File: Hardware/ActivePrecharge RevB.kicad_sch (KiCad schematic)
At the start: 59 parts, among them J1 HVConnector, J2 PrechargeContactor, J3 MainContactor, J4 ExportConnector, J5 HV+, J6 HV-, J7 Conn_01x02_Pin, U1 TLV9002QDRQ1, U2 LT1963AEST-3.3#TRPBF

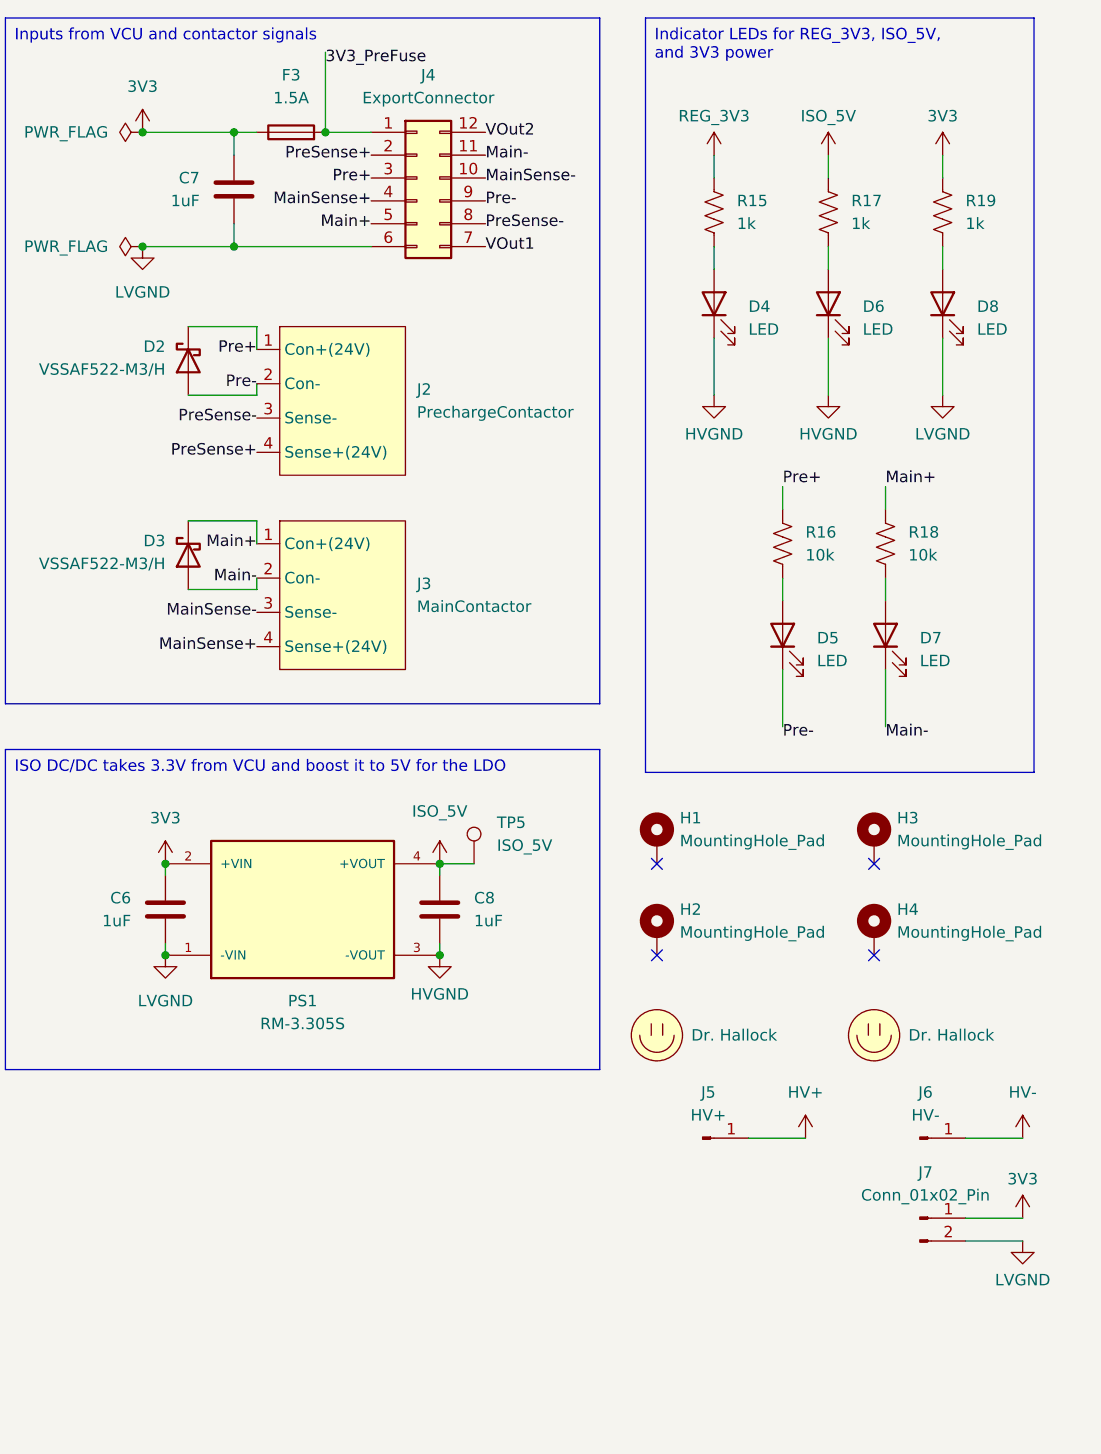
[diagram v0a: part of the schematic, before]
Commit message: HV Fuse update (#18)
* changed fuses to be HV fuses

* add step file

* silk screen updates
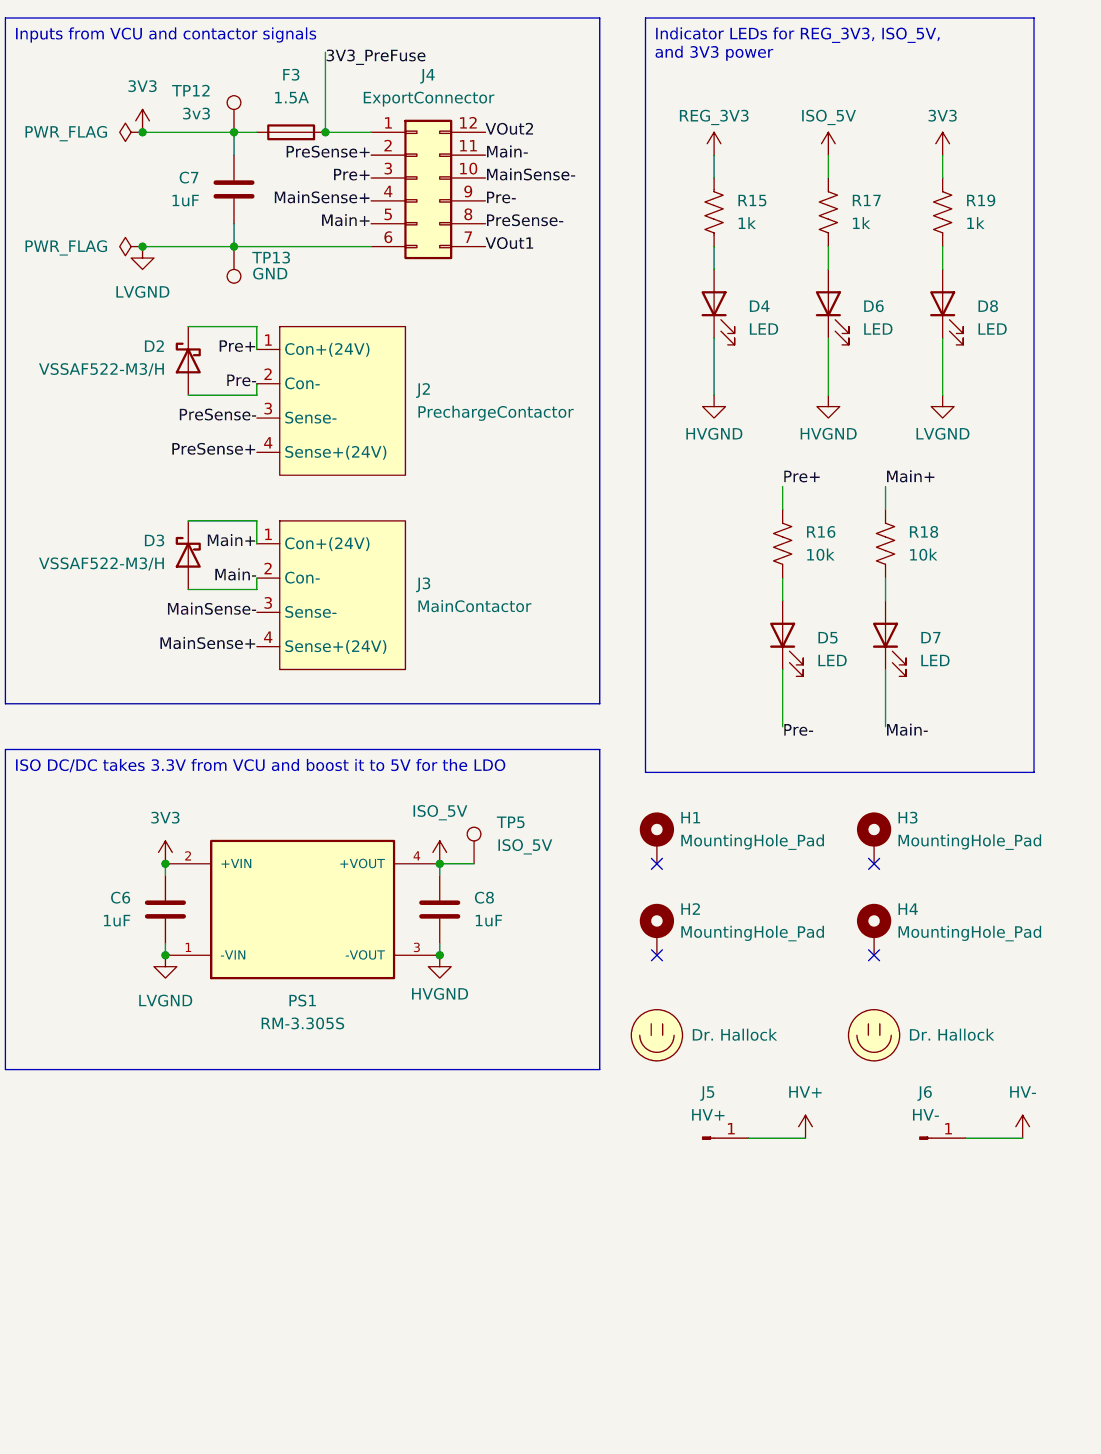
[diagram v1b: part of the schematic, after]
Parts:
- removed J7: Conn_01x02_Pin, Connector_PinHeader_2.54mm:PinHeader_1x02_P2.54mm_Vertical, symbol Connector:Conn_01x02_Pin
- added TP12: 3v3, TestPoint:TestPoint_Keystone_5005-5009_Compact, symbol Connector:TestPoint
- added TP13: GND, TestPoint:TestPoint_Keystone_5005-5009_Compact, symbol Connector:TestPoint
- F1, F2: footprint ActivePrecharge-RevB:FUSE_3568 -> UTSVT-Power:HV-Fuse
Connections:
- net 3V3: now also TP12.1
- net LVGND: now also TP13.1
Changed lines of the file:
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@@
 	(wire
 		(pts
-			(xy 269.24 152.4) (xy 275.59 152.4)
-		)
-		(stroke
-			(width 0)
-			(type default)
-		)
-	)
-	(wire
-		(pts
 			(xy 105.41 180.34) (xy 105.41 184.15)
 		)
@@
 	(wire
 		(pts
-			(xy 269.24 154.94) (xy 275.59 154.94)
-		)
-		(stroke
-			(width 0)
-			(type default)
-		)
-	)
-	(wire
-		(pts
 			(xy 71.12 81.28) (xy 71.12 92.71)
 		)
@@
 	)
 	(symbol
-		(lib_id "power:GND")
-		(at 275.59 154.94 0)
-		(unit 1)
-		(exclude_from_sim no)
-		(in_bom yes)
-		(on_board yes)
-		(dnp no)
-		(fields_autoplaced yes)
-		(property "Reference" "#PWR032"
-			(at 275.59 161.29 0)
-			(effects
-				(font
-					(size 1.27 1.27)
-				)
-				(hide yes)
-			)
-		)
-		(property "Value" "LVGND"
-			(at 275.59 160.02 0)
-			(do_not_autoplace yes)
-			(effects
-				(font
-					(size 1.27 1.27)
-				)
-				(justify bottom)
-			)
-		)
-		(property "Footprint" ""
-			(at 275.59 154.94 0)
-			(effects
-				(font
-					(size 1.27 1.27)
-				)
-				(hide yes)
-			)
-		)
-		(property "Datasheet" ""
-			(at 275.59 154.94 0)
-			(effects
-				(font
-					(size 1.27 1.27)
-				)
-				(hide yes)
-			)
-		)
-		(property "Description" "Power symbol creates a global label with name \"GND\" , ground"
-			(at 275.59 154.94 0)
-			(effects
-				(font
-					(size 1.27 1.27)
-				)
-				(hide yes)
-			)
-		)
-		(pin "1"
-		)
-		(instances
-			(project "ActivePrecharge RevB"
-				(path "/5b79bd62-039b-48b8-a776-6011f31800bf"
-					(reference "#PWR032")
-					(unit 1)
-				)
-			)
-		)
-	)
-	(symbol
 		(lib_id "Device:R_US")
 		(at 248.92 77.47 0)
@@
 	)
 	(symbol
+		(lib_id "Connector:TestPoint")
+		(at 187.96 31.75 0)
+		(unit 1)
+		(exclude_from_sim no)
+		(in_bom no)
+		(on_board yes)
+		(dnp no)
+		(property "Reference" "TP12"
+			(at 185.42 27.1779 0)
+			(effects
+				(font
+					(size 1.27 1.27)
+				)
+				(justify right)
+			)
+		)
+		(property "Value" "3v3"
+			(at 185.42 29.7179 0)
+			(effects
+				(font
+					(size 1.27 1.27)
+				)
+				(justify right)
+			)
+		)
+		(property "Footprint" "TestPoint:TestPoint_Keystone_5005-5009_Compact"
+			(at 193.04 31.75 0)
+			(effects
+				(font
+					(size 1.27 1.27)
+				)
+				(hide yes)
+			)
+		)
+		(property "Datasheet" "~"
+			(at 193.04 31.75 0)
+			(effects
+				(font
+					(size 1.27 1.27)
+				)
+				(hide yes)
+			)
+		)
+		(property "Description" "test point"
+			(at 187.96 31.75 0)
+			(effects
+				(font
+					(size 1.27 1.27)
+				)
+				(hide yes)
+			)
+		)
+		(property "Sim.Device" ""
+			(at 187.96 31.75 0)
+			(effects
+				(font
+					(size 1.27 1.27)
+				)
+				(hide yes)
+			)
+		)
+		(property "Sim.Library" ""
+			(at 187.96 31.75 0)
+			(effects
+				(font
+					(size 1.27 1.27)
+				)
+				(hide yes)
+			)
+		)
+		(property "Sim.Name" ""
+			(at 187.96 31.75 0)
+			(effects
+				(font
+					(size 1.27 1.27)
+				)
+				(hide yes)
+			)
+		)
+		(pin "1"
+		)
+		(instances
+			(project "ActivePrecharge RevB"
+				(path "/5b79bd62-039b-48b8-a776-6011f31800bf"
+					(reference "TP12")
+					(unit 1)
+				)
+			)
+		)
+	)
+	(symbol
 		(lib_id "power:+3.3V")
 		(at 139.7 105.41 0)
@@
 			)
 		)
-		(property "Footprint" "ActivePrecharge-RevB:FUSE_3568"
+		(property "Footprint" "UTSVT-Power:HV-Fuse"
 			(at 43.18 58.928 90)
 			(effects
@@
 			)
 		)
-		(property "Footprint" "ActivePrecharge-RevB:FUSE_3568"
+		(property "Footprint" "UTSVT-Power:HV-Fuse"
 			(at 43.18 33.528 90)
 			(effects
@@
 	)
 	(symbol
-		(lib_id "Connector:Conn_01x02_Pin")
-		(at 264.16 152.4 0)
+		(lib_id "Connector:TestPoint")
+		(at 187.96 44.45 180)
 		(unit 1)
 		(exclude_from_sim no)
-		(in_bom yes)
+		(in_bom no)
 		(on_board yes)
 		(dnp no)
-		(fields_autoplaced yes)
-		(property "Reference" "J7"
-			(at 264.795 147.32 0)
+		(property "Reference" "TP13"
+			(at 189.992 45.7199 0)
 			(effects
 				(font
 					(size 1.27 1.27)
 				)
+				(justify right)
 			)
 		)
-		(property "Value" "Conn_01x02_Pin"
-			(at 264.795 149.86 0)
+		(property "Value" "GND"
+			(at 189.992 47.498 0)
 			(effects
 				(font
 					(size 1.27 1.27)
 				)
+				(justify right)
 			)
 		)
-		(property "Footprint" "Connector_PinHeader_2.54mm:PinHeader_1x02_P2.54mm_Vertical"
-			(at 264.16 152.4 0)
+		(property "Footprint" "TestPoint:TestPoint_Keystone_5005-5009_Compact"
+			(at 182.88 44.45 0)
 			(effects
 				(font
@@
 		)
 		(property "Datasheet" "~"
-			(at 264.16 152.4 0)
+			(at 182.88 44.45 0)
 			(effects
 				(font
@@
 			)
 		)
-		(property "Description" "Generic connector, single row, 01x02, script generated"
-			(at 264.16 152.4 0)
+		(property "Description" "test point"
+			(at 187.96 44.45 0)
 			(effects
 				(font
@@
 		)
 		(property "Sim.Device" ""
-			(at 264.16 152.4 0)
+			(at 187.96 44.45 0)
 			(effects
 				(font
@@
 		)
 		(property "Sim.Library" ""
-			(at 264.16 152.4 0)
+			(at 187.96 44.45 0)
 			(effects
 				(font
@@
 		)
 		(property "Sim.Name" ""
-			(at 264.16 152.4 0)
-			(effects
-				(font
-					(size 1.27 1.27)
-				)
-				(hide yes)
-			)
-		)
-		(pin "2"
-		)
-		(pin "1"
-		)
-		(instances
-			(project "ActivePrecharge RevB"
-				(path "/5b79bd62-039b-48b8-a776-6011f31800bf"
-					(reference "J7")
-					(unit 1)
-				)
-			)
-		)
-	)
-	(symbol
-		(lib_id "power:+3.3V")
-		(at 275.59 152.4 0)
-		(unit 1)
-		(exclude_from_sim no)
-		(in_bom yes)
-		(on_board yes)
-		(dnp no)
-		(fields_autoplaced yes)
-		(property "Reference" "#PWR031"
-			(at 275.59 156.21 0)
-			(effects
-				(font
-					(size 1.27 1.27)
-				)
-				(hide yes)
-			)
-		)
-		(property "Value" "3V3"
-			(at 275.59 147.32 0)
-			(do_not_autoplace yes)
-			(effects
-				(font
-					(size 1.27 1.27)
-				)
-				(justify top)
-			)
-		)
-		(property "Footprint" ""
-			(at 275.59 152.4 0)
-			(effects
-				(font
-					(size 1.27 1.27)
-				)
-				(hide yes)
-			)
-		)
-		(property "Datasheet" ""
-			(at 275.59 152.4 0)
-			(effects
-				(font
-					(size 1.27 1.27)
-				)
-				(hide yes)
-			)
-		)
-		(property "Description" "Power symbol creates a global label with name \"+3.3V\""
-			(at 275.59 152.4 0)
+			(at 187.96 44.45 0)
 			(effects
 				(font
@@
 			(project "ActivePrecharge RevB"
 				(path "/5b79bd62-039b-48b8-a776-6011f31800bf"
-					(reference "#PWR031")
+					(reference "TP13")
 					(unit 1)
 				)
